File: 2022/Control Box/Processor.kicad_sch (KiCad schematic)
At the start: 57 parts, among them J401 Conn_02x05_Odd_Even, J402 Conn_01x06, J403 Conn_01x06, J404 Mini USB, SW401 SMD Tactile, SW402 SMD Tactile, SW403 SMD Tactile, SW404 SMD Tactile, U401 ESP32-WROOM, U402 STM32F405VGTx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

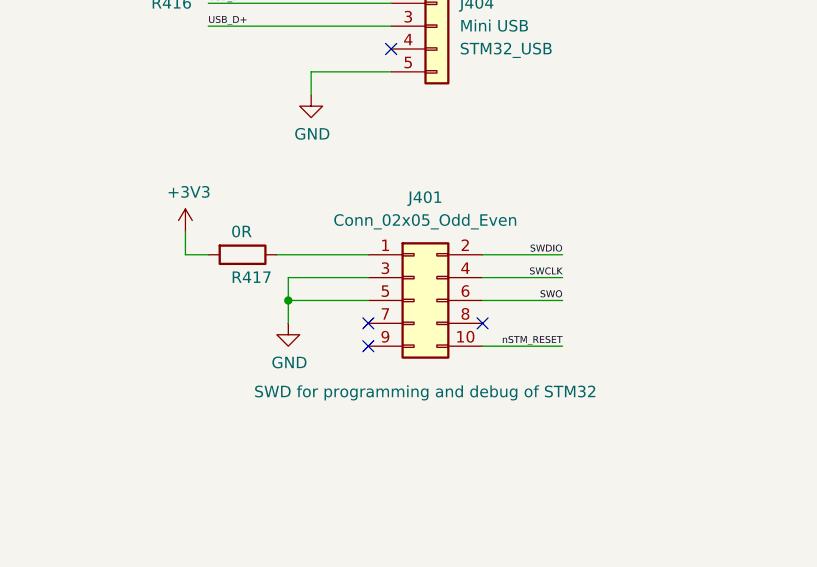
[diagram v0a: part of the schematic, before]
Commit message: rewired pcb nee to sort diff pairs
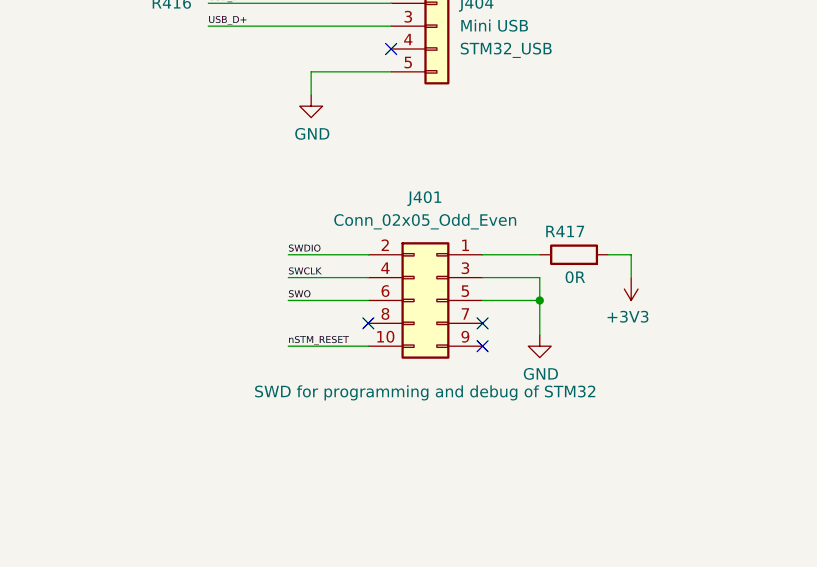
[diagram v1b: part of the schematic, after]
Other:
- moved on the sheet: R417
